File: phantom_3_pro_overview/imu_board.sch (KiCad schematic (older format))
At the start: 0 parts

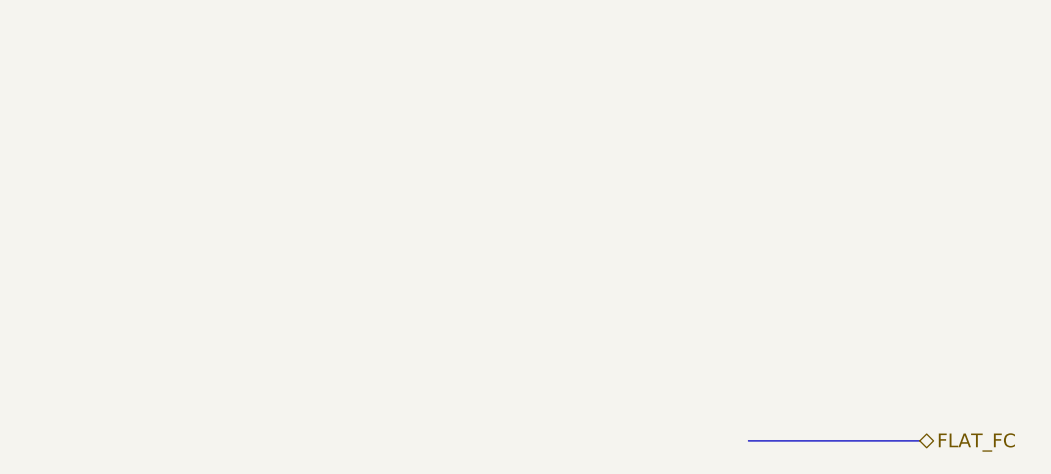
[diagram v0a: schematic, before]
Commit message: Overview: Conceptual schematics of some components.
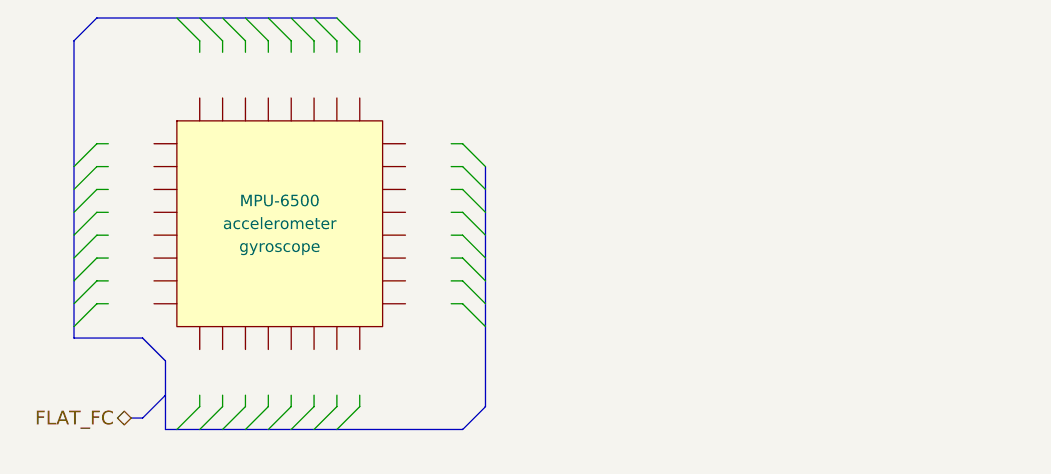
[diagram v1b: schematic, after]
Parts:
- added U?: MPU-6500, accelerometer, symbol IC_PQFP32
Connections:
- wire segments 0 -> 32
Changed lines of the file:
@@
 LIBS:valves
 LIBS:motors
+LIBS:ic_dil_generic
+LIBS:sensors
+LIBS:u-blox
+LIBS:amplifiers
 LIBS:phantom_3_pro_overview-cache
 EELAYER 25 0
 EELAYER END
-$Descr A4 11693 8268
+$Descr User 5197 4331
 encoding utf-8
-Sheet 14 23
-Title ""
+Sheet 10 23
+Title "Overview of the Phantom 3 Pro IMU board"
 Date ""
 Rev ""
 Comp ""
-Comment1 ""
+Comment1 "This schematic does not aim to be electrically correct, it is conceptual."
 Comment2 ""
 Comment3 ""
 Comment4 ""
 $EndDescr
+Text HLabel 1000 2350 0    60   BiDi ~ 0
+FLAT_FC
+$Comp
+L IC_PQFP32 U?
+U 1 1 596E807B
+P 1650 1500
+F 0 "U?" H 1650 1400 50  0001 C CNN
+F 1 "MPU-6500" H 1650 1600 50  0000 C CNN
+F 2 "accelerometer" H 1650 1500 50  0000 C CNN
+F 3 "gyroscope" H 1650 1400 50  0000 C CNN
+	1    1650 1500
+	1    0    0    -1
+$EndComp
+Entry Wire Line
+	1300 2400 1400 2300
+Entry Wire Line
+	1400 2400 1500 2300
+Entry Wire Line
+	1500 2400 1600 2300
+Entry Wire Line
+	1600 2400 1700 2300
+Entry Wire Line
+	1700 2400 1800 2300
+Entry Wire Line
+	1800 2400 1900 2300
+Entry Wire Line
+	1200 2400 1300 2300
+Entry Wire Line
+	1900 2400 2000 2300
+Wire Wire Line
+	2000 2300 2000 2250
+Wire Wire Line
+	1900 2250 1900 2300
+Wire Wire Line
+	1800 2300 1800 2250
+Wire Wire Line
+	1700 2250 1700 2300
+Wire Wire Line
+	1600 2300 1600 2250
+Wire Wire Line
+	1500 2250 1500 2300
+Wire Wire Line
+	1400 2300 1400 2250
+Wire Wire Line
+	1300 2250 1300 2300
+Entry Wire Line
+	2550 1850 2450 1750
+Entry Wire Line
+	2550 1750 2450 1650
+Entry Wire Line
+	2550 1650 2450 1550
+Entry Wire Line
+	2550 1550 2450 1450
+Entry Wire Line
+	2550 1450 2450 1350
+Entry Wire Line
+	2550 1350 2450 1250
+Entry Wire Line
+	2550 1950 2450 1850
+Entry Wire Line
+	2550 1250 2450 1150
+Wire Wire Line
+	2450 1150 2400 1150
+Wire Wire Line
+	2400 1250 2450 1250
+Wire Wire Line
+	2450 1350 2400 1350
+Wire Wire Line
+	2400 1450 2450 1450
+Wire Wire Line
+	2450 1550 2400 1550
+Wire Wire Line
+	2400 1650 2450 1650
+Wire Wire Line
+	2450 1750 2400 1750
+Wire Wire Line
+	2400 1850 2450 1850
+Entry Wire Line
+	850  1750 750  1850
+Entry Wire Line
+	850  1650 750  1750
+Entry Wire Line
+	850  1550 750  1650
+Entry Wire Line
+	850  1450 750  1550
+Entry Wire Line
+	850  1350 750  1450
+Entry Wire Line
+	850  1250 750  1350
+Entry Wire Line
+	850  1850 750  1950
+Entry Wire Line
+	850  1150 750  1250
+Wire Wire Line
+	900  1150 850  1150
+Wire Wire Line
+	850  1250 900  1250
+Wire Wire Line
+	900  1350 850  1350
+Wire Wire Line
+	850  1450 900  1450
+Wire Wire Line
+	900  1550 850  1550
+Wire Wire Line
+	850  1650 900  1650
+Wire Wire Line
+	900  1750 850  1750
+Wire Wire Line
+	850  1850 900  1850
+Entry Wire Line
+	1800 600  1900 700
+Entry Wire Line
+	1700 600  1800 700
+Entry Wire Line
+	1600 600  1700 700
+Entry Wire Line
+	1500 600  1600 700
+Entry Wire Line
+	1400 600  1500 700
+Entry Wire Line
+	1300 600  1400 700
+Entry Wire Line
+	1900 600  2000 700
+Entry Wire Line
+	1200 600  1300 700
+Wire Wire Line
+	1300 700  1300 750
+Wire Wire Line
+	1400 750  1400 700
+Wire Wire Line
+	1500 700  1500 750
+Wire Wire Line
+	1600 750  1600 700
+Wire Wire Line
+	1700 700  1700 750
+Wire Wire Line
+	1800 750  1800 700
+Wire Wire Line
+	1900 700  1900 750
+Wire Wire Line
+	2000 750  2000 700
+Entry Bus Bus
+	2450 2400 2550 2300
 Wire Bus Line
-	4450 2450 3700 2450
-Text HLabel 4450 2450 2    60   BiDi ~ 0
-FLAT_FC
+	2550 1250 2550 2300
+Entry Bus Bus
+	750  700  850  600
+Wire Bus Line
+	850  600  1900 600
+Entry Bus Bus
+	1050 2000 1150 2100
+Entry Bus Bus
+	1050 2350 1150 2250
+Wire Bus Line
+	1050 2000 750  2000
+Wire Bus Line
+	1150 2100 1150 2400
+Wire Bus Line
+	1150 2400 2450 2400
+Wire Bus Line
+	750  2000 750  700
+Wire Bus Line
+	1000 2350 1050 2350
 $EndSCHEMATC

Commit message: Overview: Added OFDM board.
Besides drawing the OFDM, components were updated.
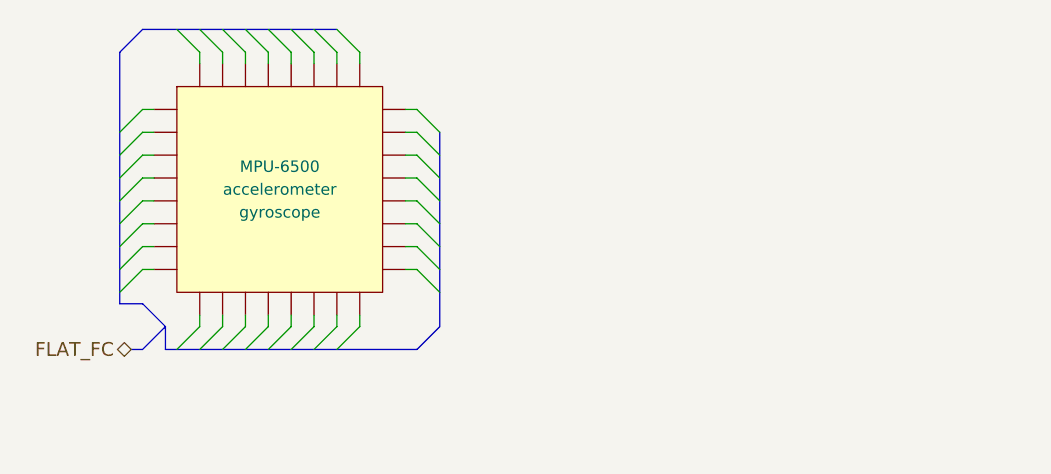
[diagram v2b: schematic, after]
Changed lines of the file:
@@
 LIBS:u-blox
 LIBS:amplifiers
+LIBS:transistors-switches
 LIBS:phantom_3_pro_overview-cache
 EELAYER 25 0
@@
 Comment4 ""
 $EndDescr
-Text HLabel 1000 2350 0    60   BiDi ~ 0
+Text HLabel 1000 2050 0    60   BiDi ~ 0
 FLAT_FC
 $Comp
 L IC_PQFP32 U?
 U 1 1 596E807B
-P 1650 1500
-F 0 "U?" H 1650 1400 50  0001 C CNN
-F 1 "MPU-6500" H 1650 1600 50  0000 C CNN
-F 2 "accelerometer" H 1650 1500 50  0000 C CNN
-F 3 "gyroscope" H 1650 1400 50  0000 C CNN
-	1    1650 1500
+P 1650 1350
+F 0 "U?" H 1650 1250 50  0001 C CNN
+F 1 "MPU-6500" H 1650 1450 50  0000 C CNN
+F 2 "accelerometer" H 1650 1350 50  0000 C CNN
+F 3 "gyroscope" H 1650 1250 50  0000 C CNN
+	1    1650 1350
 	1    0    0    -1
 $EndComp
 Entry Wire Line
-	1300 2400 1400 2300
+	1300 2050 1400 1950
 Entry Wire Line
-	1400 2400 1500 2300
+	1400 2050 1500 1950
 Entry Wire Line
-	1500 2400 1600 2300
+	1500 2050 1600 1950
 Entry Wire Line
-	1600 2400 1700 2300
+	1600 2050 1700 1950
 Entry Wire Line
-	1700 2400 1800 2300
+	1700 2050 1800 1950
 Entry Wire Line
-	1800 2400 1900 2300
+	1800 2050 1900 1950
 Entry Wire Line
-	1200 2400 1300 2300
+	1200 2050 1300 1950
 Entry Wire Line
-	1900 2400 2000 2300
+	1900 2050 2000 1950
 Wire Wire Line
-	2000 2300 2000 2250
+	2000 1950 2000 1900
 Wire Wire Line
-	1900 2250 1900 2300
+	1900 1900 1900 1950
 Wire Wire Line
-	1800 2300 1800 2250
+	1800 1950 1800 1900
 Wire Wire Line
-	1700 2250 1700 2300
+	1700 1900 1700 1950
 Wire Wire Line
-	1600 2300 1600 2250
+	1600 1950 1600 1900
 Wire Wire Line
-	1500 2250 1500 2300
+	1500 1900 1500 1950
 Wire Wire Line
-	1400 2300 1400 2250
+	1400 1950 1400 1900
 Wire Wire Line
-	1300 2250 1300 2300
+	1300 1900 1300 1950
 Entry Wire Line
-	2550 1850 2450 1750
+	2350 1700 2250 1600
 Entry Wire Line
-	2550 1750 2450 1650
+	2350 1600 2250 1500
 Entry Wire Line
-	2550 1650 2450 1550
+	2350 1500 2250 1400
 Entry Wire Line
-	2550 1550 2450 1450
+	2350 1400 2250 1300
 Entry Wire Line
-	2550 1450 2450 1350
+	2350 1300 2250 1200
 Entry Wire Line
-	2550 1350 2450 1250
+	2350 1200 2250 1100
 Entry Wire Line
-	2550 1950 2450 1850
+	2350 1800 2250 1700
 Entry Wire Line
-	2550 1250 2450 1150
+	2350 1100 2250 1000
 Wire Wire Line
-	2450 1150 2400 1150
+	2250 1000 2200 1000
 Wire Wire Line
-	2400 1250 2450 1250
+	2200 1100 2250 1100
 Wire Wire Line
-	2450 1350 2400 1350
+	2250 1200 2200 1200
 Wire Wire Line
-	2400 1450 2450 1450
+	2200 1300 2250 1300
 Wire Wire Line
-	2450 1550 2400 1550
+	2250 1400 2200 1400
 Wire Wire Line
-	2400 1650 2450 1650
+	2200 1500 2250 1500
 Wire Wire Line
-	2450 1750 2400 1750
+	2250 1600 2200 1600
 Wire Wire Line
-	2400 1850 2450 1850
+	2200 1700 2250 1700
 Entry Wire Line
-	850  1750 750  1850
+	1050 1600 950  1700
 Entry Wire Line
-	850  1650 750  1750
+	1050 1500 950  1600
 Entry Wire Line
-	850  1550 750  1650
+	1050 1400 950  1500
 Entry Wire Line
-	850  1450 750  1550
+	1050 1300 950  1400
 Entry Wire Line
-	850  1350 750  1450
+	1050 1200 950  1300
 Entry Wire Line
-	850  1250 750  1350
+	1050 1100 950  1200
 Entry Wire Line
-	850  1850 750  1950
+	1050 1700 950  1800
 Entry Wire Line
-	850  1150 750  1250
+	1050 1000 950  1100
 Wire Wire Line
-	900  1150 850  1150
+	1100 1000 1050 1000
 Wire Wire Line
-	850  1250 900  1250
+	1050 1100 1100 1100
 Wire Wire Line
-	900  1350 850  1350
+	1100 1200 1050 1200
 Wire Wire Line
-	850  1450 900  1450
+	1050 1300 1100 1300
 Wire Wire Line
-	900  1550 850  1550
+	1100 1400 1050 1400
 Wire Wire Line
-	850  1650 900  1650
+	1050 1500 1100 1500
 Wire Wire Line
-	900  1750 850  1750
+	1100 1600 1050 1600
 Wire Wire Line
-	850  1850 900  1850
+	1050 1700 1100 1700
 Entry Wire Line
-	1800 600  1900 700
+	1800 650  1900 750
 Entry Wire Line
-	1700 600  1800 700
+	1700 650  1800 750
 Entry Wire Line
-	1600 600  1700 700
+	1600 650  1700 750
 Entry Wire Line
-	1500 600  1600 700
+	1500 650  1600 750
 Entry Wire Line
-	1400 600  1500 700
+	1400 650  1500 750
 Entry Wire Line
-	1300 600  1400 700
+	1300 650  1400 750
 Entry Wire Line
-	1900 600  2000 700
+	1900 650  2000 750
 Entry Wire Line
-	1200 600  1300 700
+	1200 650  1300 750
 Wire Wire Line
-	1300 700  1300 750
+	1300 750  1300 800
 Wire Wire Line
-	1400 750  1400 700
+	1400 800  1400 750
 Wire Wire Line
-	1500 700  1500 750
+	1500 750  1500 800
 Wire Wire Line
-	1600 750  1600 700
+	1600 800  1600 750
 Wire Wire Line
-	1700 700  1700 750
+	1700 750  1700 800
 Wire Wire Line
-	1800 750  1800 700
+	1800 800  1800 750
 Wire Wire Line
-	1900 700  1900 750
+	1900 750  1900 800
 Wire Wire Line
-	2000 750  2000 700
+	2000 800  2000 750
 Entry Bus Bus
-	2450 2400 2550 2300
+	2250 2050 2350 1950
+Entry Bus Bus
+	950  750  1050 650
+Entry Bus Bus
+	1050 1850 1150 1950
+Entry Bus Bus
+	1050 2050 1150 1950
 Wire Bus Line
-	2550 1250 2550 2300
-Entry Bus Bus
-	750  700  850  600
+	1000 2050 1050 2050
 Wire Bus Line
-	850  600  1900 600
-Entry Bus Bus
-	1050 2000 1150 2100
-Entry Bus Bus
-	1050 2350 1150 2250
+	2350 1100 2350 1950
 Wire Bus Line
-	1050 2000 750  2000
+	1150 2050 2250 2050
 Wire Bus Line
-	1150 2100 1150 2400
+	1900 650  1050 650
 Wire Bus Line
-	1150 2400 2450 2400
+	950  1850 950  750
 Wire Bus Line
-	750  2000 750  700
+	950  1850 1050 1850
 Wire Bus Line
-	1000 2350 1050 2350
+	1150 2050 1150 1950
 $EndSCHEMATC

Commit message: Overview: Upgraded to KiCAD 5.0.1.
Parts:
- U?: symbol IC_PQFP32 -> ic_dil_generic:IC_PQFP32
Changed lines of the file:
@@
-EESchema Schematic File Version 2
-LIBS:power
-LIBS:device
-LIBS:transistors
-LIBS:conn
-LIBS:linear
-LIBS:regul
-LIBS:74xx
-LIBS:cmos4000
-LIBS:adc-dac
-LIBS:memory
-LIBS:xilinx
-LIBS:microcontrollers
-LIBS:dsp
-LIBS:microchip
-LIBS:analog_switches
-LIBS:motorola
-LIBS:texas
-LIBS:intel
-LIBS:audio
-LIBS:interface
-LIBS:digital-audio
-LIBS:philips
-LIBS:display
-LIBS:cypress
-LIBS:siliconi
-LIBS:opto
-LIBS:atmel
-LIBS:contrib
-LIBS:valves
-LIBS:motors
-LIBS:ic_dil_generic
-LIBS:sensors
-LIBS:u-blox
-LIBS:amplifiers
-LIBS:transistors-switches
-LIBS:transistors-power
-LIBS:sensors-v2
-LIBS:regul-v2
+EESchema Schematic File Version 4
 LIBS:phantom_3_pro_overview-cache
-EELAYER 25 0
+EELAYER 26 0
 EELAYER END
 $Descr User 5197 4331
@@
 FLAT_FC
 $Comp
-L IC_PQFP32 U?
+L ic_dil_generic:IC_PQFP32 U?
 U 1 1 596E807B
 P 1650 1350

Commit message: All: Finished updating to KiCad 5.0.1.
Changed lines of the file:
@@
 	1000 2050 1050 2050
+Wire Bus Line
+	950  1850 1050 1850
+Wire Bus Line
+	1150 2050 1150 1950
 Wire Bus Line
 	2350 1100 2350 1950
@@
 	1150 2050 2250 2050
 Wire Bus Line
-	1900 650  1050 650
+	1050 650  1900 650
 Wire Bus Line
-	950  1850 950  750
-Wire Bus Line
-	950  1850 1050 1850
-Wire Bus Line
-	1150 2050 1150 1950
+	950  750  950  1850
 $EndSCHEMATC
